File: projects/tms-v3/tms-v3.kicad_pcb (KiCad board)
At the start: 2 copper layers, 100 x 80 mm, 66 parts, among them J1 XT60-ELEC, J2 XT60-IGN, J3 LOAD-CELL, J4 PRESSURE, J5 ARM-SW, J6 E-MATCH, J7 TEENSY-L, J8 TEENSY-R, J9 XBEE3, K1 HF46F, Q1 MMBT3904, U2 ADS1256, U3 ADS1220, U4 LM7805, Y1 7.68MHz

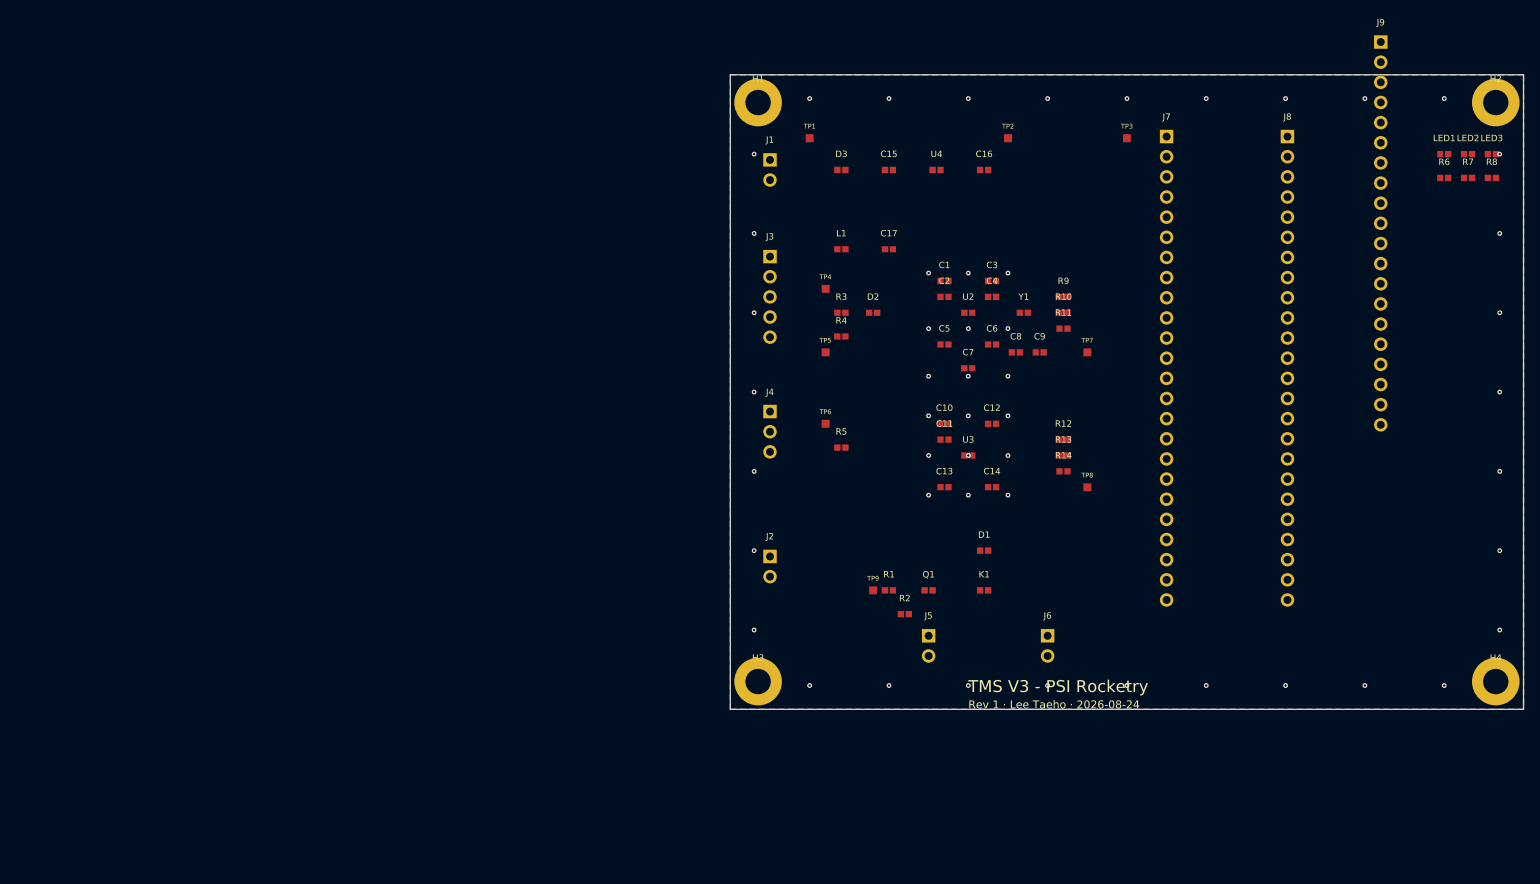
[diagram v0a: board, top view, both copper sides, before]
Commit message: PCB workspace: scoped escape hatch, hardened gates, repo cleanup
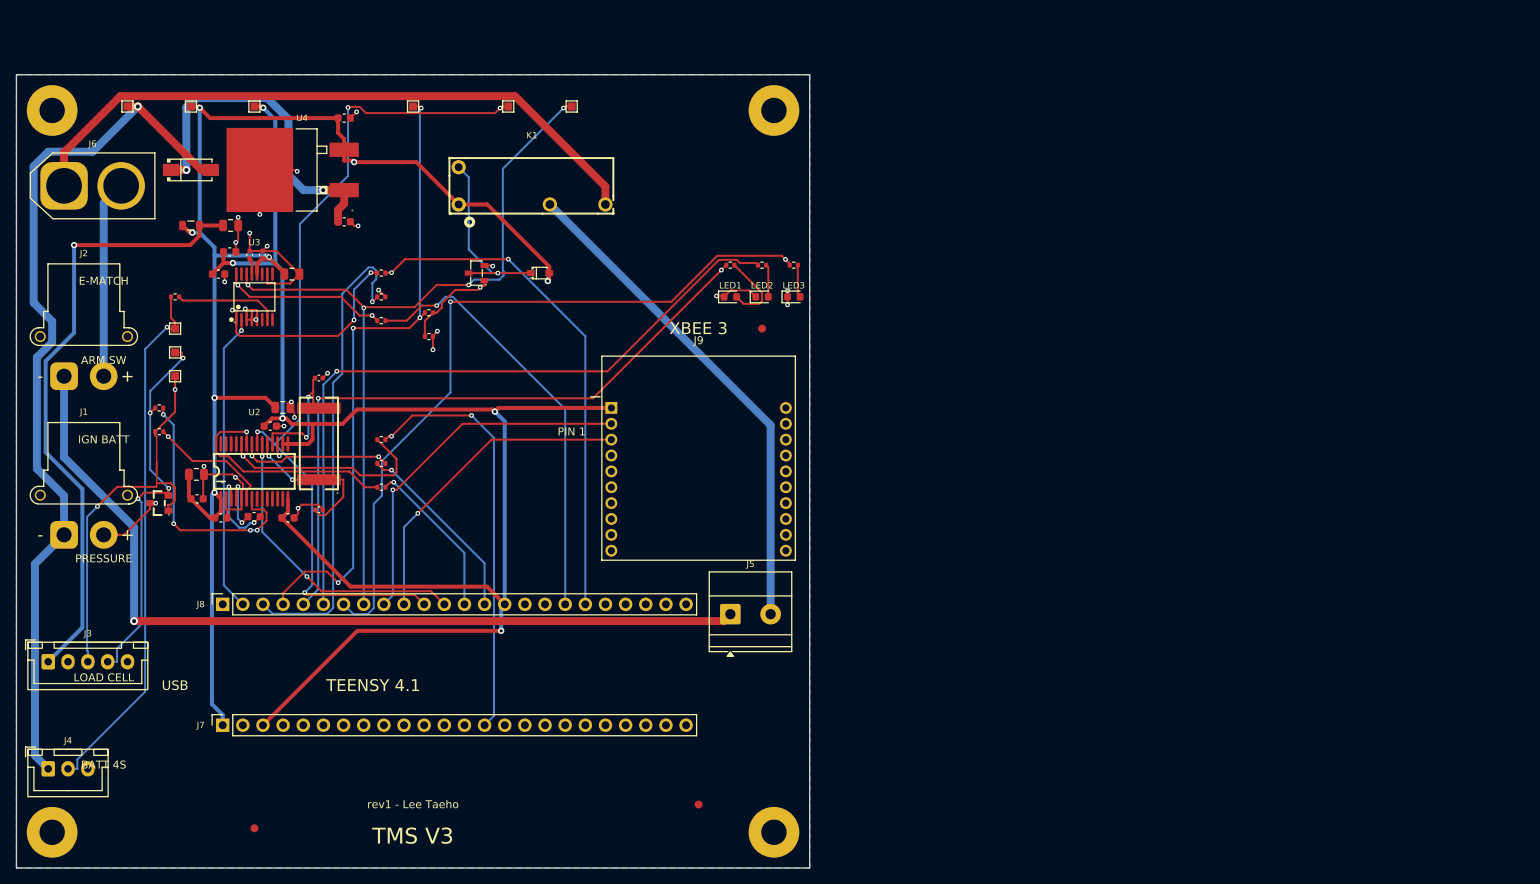
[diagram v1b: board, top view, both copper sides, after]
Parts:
- added FID1: FIDUCIAL, Fiducial:Fiducial_1mm_Mask3mm, F.Cu at (40.0, 195.0)
- added FID2: FIDUCIAL, Fiducial:Fiducial_1mm_Mask3mm, F.Cu at (96.0, 192.0)
- added FID3: FIDUCIAL, Fiducial:Fiducial_1mm_Mask3mm, F.Cu at (104.0, 132.0)
- C10, C11: footprint Capacitor_SMD:C_0603_1608Metric -> Capacitor_SMD:C_0402_1005Metric
- D1: footprint Diode_SMD:D_SOD-323 -> jlcpcb:SOD-323_L1.8-W1.3-LS2.5-RD-1
- D2: value TVS -> PESD5V0S2BT; footprint Package_TO_SOT_SMD:SOT-23 -> jlcpcb:SOT-23_L2.9-W1.3-P1.90-LS2.4-BR
- D3: footprint Diode_SMD:D_SMA -> jlcpcb:SMA_L4.4-W2.8-LS5.4-R-RD
- J1: value XT60-ELEC -> XT30PW-ELEC; footprint Connector_PinHeader_2.54mm:PinHeader_1x02_P2.54mm_Vertical -> Connector_AMASS:AMASS_XT30PW-F_1x02_P2.50mm_Horizontal
- J2: value XT60-IGN -> XT30PW-IGN; footprint Connector_PinHeader_2.54mm:PinHeader_1x02_P2.54mm_Vertical -> Connector_AMASS:AMASS_XT30PW-F_1x02_P2.50mm_Horizontal
- J3: footprint Connector_PinHeader_2.54mm:PinHeader_1x05_P2.54mm_Vertical -> Connector_JST:JST_XH_B5B-XH-A_1x05_P2.50mm_Vertical
- J4: footprint Connector_PinHeader_2.54mm:PinHeader_1x03_P2.54mm_Vertical -> Connector_JST:JST_XH_B3B-XH-A_1x03_P2.50mm_Vertical
- J5: footprint Connector_PinHeader_2.54mm:PinHeader_1x02_P2.54mm_Vertical -> TerminalBlock_Phoenix:TerminalBlock_Phoenix_MKDS-1,5-2-5.08_1x02_P5.08mm_Horizontal
- J6: value E-MATCH -> IGN-OUT; footprint Connector_PinHeader_2.54mm:PinHeader_1x02_P2.54mm_Vertical -> Connector_AMASS:AMASS_XT60-F_1x02_P7.20mm_Vertical
- J7, J8: footprint Connector_PinHeader_2.54mm:PinHeader_1x24_P2.54mm_Vertical -> Connector_PinSocket_2.54mm:PinSocket_1x24_P2.54mm_Vertical
- J9: value XBEE3 -> XBee_THT_20pin_P2.00mm; footprint Connector_PinHeader_2.54mm:PinHeader_2x10_P2.00mm_Vertical -> tms:XBee_THT_20pin_P2.00mm
- K1: value HF46F -> HF46F-G/5-HS1T; footprint Relay_THT:Relay_SPDT_HF46F -> jlcpcb:RELAYS-TH_HF46F-G-XX-HS1-XXX
- Q1: footprint Package_TO_SOT_SMD:SOT-23 -> jlcpcb:SOT-23-3_L2.9-W1.3-P1.90-LS2.4-BR
- U2: value ADS1256 -> ADS1256IDBR; footprint Package_SO:SSOP-28_5.3x10.2mm_P0.65mm -> jlcpcb:SSOP-28_L10.2-W5.3-P0.65-LS7.8-BL
- U3: value ADS1220 -> ADS1220IPWR; footprint Package_SO:TSSOP-16_4.4x5mm_P0.65mm -> jlcpcb:TSSOP-16_L5.0-W4.4-P0.65-LS6.4-BL
- U4: footprint Package_TO_SOT_SMD:TO-263-3_TabPin2 -> jlcpcb:TO-263-2_L10.1-W9.1-P5.08-LS15.2-BR-1
- Y1: footprint Crystal:Crystal_HC49-U_Vertical -> jlcpcb:CRYSTAL-SMD_L11.4-W4.7-LS12.4
- moved J8 137.5 mm to (36.0, 166.8), turned to 90 degrees
- moved J6 136.9 mm to (16.0, 114.0)
- moved J7 127.2 mm to (36.0, 182.0), turned to 90 degrees
- moved TP3 110.1 mm to (40.0, 104.0)
- moved C3 103.2 mm to (32.7, 150.4)
- moved TP2 103.1 mm to (32.0, 104.0)
- moved J3 102.0 mm to (14.0, 174.0)
- moved C14 101.2 mm to (35.5, 125.1)
- moved J4 100.4 mm to (14.0, 187.5)
- moved J1 100.2 mm to (16.0, 158.0)
- moved J9 99.5 mm to (85.0, 142.0)
- moved C2 97.6 mm to (32.8, 153.5)
- moved C1 96.0 mm to (35.8, 155.9)
- moved C13 94.9 mm to (36.9, 122.3)
- moved D2 93.1 mm to (28.0, 154.0)
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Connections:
- C11 pad 1: +5V -> +3V3
- C7 pad 1: (no net) -> VREF_P
- C7 pad 2: GND -> VREF_N
- C8 pad 1: GND -> XTAL1
- C9 pad 1: GND -> XTAL2
- D1 pad 1: (no net) -> RELAY_COIL_SW
- D1 pad 2: GND -> +5V
- D2 pad 1: (no net) -> LC_SIG_P
- D2 pad 2: GND -> LC_SIG_N
- D3 pad 1: VBAT_PROT -> VBAT
- D3 pad 2: GND -> VBAT_PROT
- H1 pad 1: GND -> (no net)
- H2 pad 1: GND -> (no net)
- H3 pad 1: GND -> (no net)
- H4 pad 1: GND -> (no net)
- J1 pad 1: (no net) -> VBAT
- J1 pad 2: (no net) -> GND
- J2 pad 1: (no net) -> IGN_BATT+
- J2 pad 2: (no net) -> IGN_GND
- J3 pad 1: (no net) -> +5V_FILT
- J3 pad 2: (no net) -> GND
- J3 pad 3: (no net) -> LC_SIG_P
- J3 pad 4: (no net) -> LC_SIG_N
- J3 pad 5: (no net) -> GND
- J4 pad 1: (no net) -> VBAT
- J4 pad 2: (no net) -> PRES_RAW
- J4 pad 3: (no net) -> GND
- J5 pad 1: (no net) -> IGN_BATT+
- J5 pad 2: (no net) -> IGN_ARM_RET
- J6 pad 1: (no net) -> IGN_OUT
- J6 pad 2: (no net) -> IGN_GND
- J7 pad 1: (no net) -> +5V
- J7 pad 14: (no net) -> SPI0_SCK
- J7 pad 15: (no net) -> GND
- J7 pad 2: (no net) -> GND
- J7 pad 3: (no net) -> +3V3
- J8 pad 1: (no net) -> GND
- J8 pad 10: (no net) -> UART2_TX
- J8 pad 11: (no net) -> ADS1256_DRDY
- J8 pad 12: (no net) -> ADS1256_CS
- J8 pad 13: (no net) -> SPI0_MOSI
- J8 pad 14: (no net) -> SPI0_MISO
- J8 pad 15: (no net) -> +3V3
- J8 pad 18: (no net) -> SPI1_MOSI
- J8 pad 19: (no net) -> SPI1_SCK
- J8 pad 2: (no net) -> ADS1220_CS
- J8 pad 3: (no net) -> SPI1_MISO
- J8 pad 4: (no net) -> RELAY_CTRL
- J8 pad 5: (no net) -> LED_PWR
- J8 pad 6: (no net) -> LED_ARM
- J8 pad 7: (no net) -> LED_TX
- J8 pad 8: (no net) -> ADS1220_DRDY
- J8 pad 9: (no net) -> UART2_RX
- J9 pad 1: (no net) -> +3V3
- J9 pad 10: (no net) -> GND
- J9 pad 2: (no net) -> UART2_RX
- J9 pad 3: (no net) -> UART2_TX
- K1 pad 1: (no net) -> +5V
- K1 pad 2: GND -> IGN_ARM_RET
- L1 pad 2: GND -> +5V_FILT
- LED1 pad 1: LED_PWR -> GND
- LED1 pad 2: GND -> LED_PWR_A
- LED2 pad 1: LED_ARM -> GND
- LED2 pad 2: GND -> LED_ARM_A
- LED3 pad 1: LED_TX -> GND
- LED3 pad 2: GND -> LED_TX_A
- Q1 pad 1: GND -> NPN_BASE
- R1 pad 2: GND -> NPN_BASE
- R10 pad 2: GND -> ADS1256_DOUT_ADC
- R11 pad 1: SPI0_SCK -> ADS1256_SCLK_ADC
- R11 pad 2: GND -> SPI0_SCK
- R12 pad 1: SPI1_MOSI -> ADS1220_DIN_ADC
- R12 pad 2: GND -> SPI1_MOSI
- R13 pad 2: GND -> ADS1220_DOUT_ADC
- R14 pad 1: SPI1_SCK -> ADS1220_SCLK_ADC
- R14 pad 2: GND -> SPI1_SCK
- R2 pad 1: GND -> NPN_BASE
- R3 pad 1: LC_AINP -> LC_SIG_P
- R3 pad 2: GND -> LC_AINP
- R4 pad 1: LC_AINN -> LC_SIG_N
- R4 pad 2: GND -> LC_AINN
- R5 pad 1: PRES_SIG -> PRES_RAW
- R5 pad 2: GND -> PRES_SIG
- R6 pad 2: GND -> LED_PWR_A
- R7 pad 2: GND -> LED_ARM_A
- R8 pad 2: GND -> LED_TX_A
- R9 pad 1: SPI0_MOSI -> ADS1256_DIN_ADC
- R9 pad 2: GND -> SPI0_MOSI
- TP4 pad 1: LC_AINP -> LC_SIG_P
- TP5 pad 1: LC_AINN -> LC_SIG_N
- TP6 pad 1: PRES_SIG -> PRES_RAW
- U2 pad 1: (no net) -> +5V
- U3 pad 1: (no net) -> ADS1220_SCLK_ADC
- U3 pad 2: GND -> ADS1220_CS
- U4 pad 1: +5V -> VBAT_PROT
- Y1 pad 1: (no net) -> XTAL1
- Y1 pad 2: GND -> XTAL2
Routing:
- net +3V3: track 0.00 -> 203.5 mm, vias 0 -> 5
- net +5V: track 0.00 -> 172.2 mm, vias 0 -> 7
- net VBAT: track 0.00 -> 111.4 mm, vias 0 -> 1
- net IGN_BATT+: track 0.00 -> 110.1 mm, vias 0 -> 1
- net ADS1256_DRDY: track 0.00 -> 108.3 mm, vias 0 -> 4
- net ADS1220_DRDY: track 0.00 -> 99.3 mm, vias 0 -> 4
- net LED_TX: track 0.00 -> 93.0 mm, vias 0 -> 2
- net LED_ARM: track 0.00 -> 89.3 mm, vias 0 -> 1
- net GND: track 0.00 -> 88.3 mm, vias 50 -> 26
- net LED_PWR: track 0.00 -> 85.2 mm, vias 0 -> 2
- net IGN_OUT: track 0.00 -> 82.4 mm
- net RELAY_CTRL: track 0.00 -> 80.4 mm, vias 0 -> 4
- net +5V_FILT: track 0.00 -> 78.3 mm, vias 0 -> 1
- net PRES_RAW: track 0.00 -> 66.8 mm, vias 0 -> 1
- net SPI1_SCK: track 0.00 -> 63.8 mm, vias 0 -> 2
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- removed copper zone on F.Cu, net GND
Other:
- board size 100 x 80 mm -> 100 x 100 mm
- rule pad_to_mask_clearance: 0.05 -> 0
- board text added: "ARM SW"
- board text added: "BATT 4S"
- board text added: "E-MATCH"
- board text added: "IGN BATT"
- board text added: "LOAD CELL"
- board text added: "PIN 1"
- board text added: "PRESSURE"
- board text added: "TEENSY 4.1"
- board text added: "TMS V3"
- board text added: "USB"
- board text added: "XBEE 3"
- board text added: "rev1 - Lee Taeho"
- board text removed: "ANALOG"
- board text removed: "DIGITAL"
- board text removed: "IGNITION"
- board text removed: "POWER"
- board text removed: "RF"
- board text removed: "Rev 1 · Lee Taeho · 2026-08-24"
- board text removed: "TMS V3 - PSI Rocketry"

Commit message: 9/6 update
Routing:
- net VBAT: track 111.4 -> 45.5 mm, vias 1 -> 0
- net PRES_RAW: track 66.8 -> 4.21 mm, vias 1 -> 0
- net ADS1220_DOUT_ADC: track 1.21 -> 20.1 mm, vias 1 -> 0
- net ADS1256_SCLK_ADC: track 27.2 -> 43.0 mm, vias 1 -> 2
- net LED_TX: track 93.0 -> 107.0 mm, vias 2 -> 3
- net ADS1256_DRDY: track 108.3 -> 98.4 mm
- net SPI0_SCK: track 52.8 -> 44.0 mm, vias 2 -> 1
- net LC_AINN: track 32.1 -> 25.8 mm, vias 4 -> 2
- net SPI1_SCK: track 63.8 -> 57.9 mm, vias 2 -> 1
- net SPI0_MISO: track 23.9 -> 28.8 mm
- net +3V3: track 203.5 -> 208.2 mm, vias 5 -> 6
- net ADS1256_CS: track 37.8 -> 42.5 mm
- net XTAL2: track 16.2 -> 12.7 mm, vias 2 -> 0
- net SPI1_MISO: track 60.5 -> 57.6 mm
- net UART2_TX: track 40.4 -> 43.1 mm
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
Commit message: feat: promote TMS hierarchy with safe board net reconciliation
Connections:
- net ADS1220_DIN_ADC renamed ADS1220 pressure/ADS1220_DIN_ADC
- net ADS1220_DOUT_ADC renamed ADS1220 pressure/ADS1220_DOUT_ADC
- net ADS1220_SCLK_ADC renamed ADS1220 pressure/ADS1220_SCLK_ADC
- net ADS1256_DIN_ADC renamed ADS1256 load cell/ADS1256_DIN_ADC
- net ADS1256_DOUT_ADC renamed ADS1256 load cell/ADS1256_DOUT_ADC
- net ADS1256_SCLK_ADC renamed ADS1256 load cell/ADS1256_SCLK_ADC
- net IGN_BATT+ renamed Connectors and test/IGN_BATT+
- net IGN_GND renamed Connectors and test/IGN_GND
- net LC_AINN renamed ADS1256 load cell/LC_AINN
- net LC_AINP renamed ADS1256 load cell/LC_AINP
- net LED_ARM renamed Controller and telemetry/LED_ARM
- net LED_ARM_A renamed Controller and telemetry/LED_ARM_A
- net LED_PWR renamed Controller and telemetry/LED_PWR
- net LED_PWR_A renamed Controller and telemetry/LED_PWR_A
- net LED_TX renamed Controller and telemetry/LED_TX
- net LED_TX_A renamed Controller and telemetry/LED_TX_A
- net NPN_BASE renamed Ignition/NPN_BASE
- net PRES_SIG renamed ADS1220 pressure/PRES_SIG
- net RELAY_COIL_SW renamed Ignition/RELAY_COIL_SW
- net UART2_RX renamed Controller and telemetry/UART2_RX
- net UART2_TX renamed Controller and telemetry/UART2_TX
- net VBAT_PROT renamed Power/VBAT_PROT
- net VREF_N renamed ADS1256 load cell/VREF_N
- net VREF_P renamed ADS1256 load cell/VREF_P
- net XTAL1 renamed ADS1256 load cell/XTAL1
- net XTAL2 renamed ADS1256 load cell/XTAL2

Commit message: batch
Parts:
- C8, C9: value 22pF -> 33pF
- J9: value XBee_THT_20pin_P2.00mm -> XBEE3
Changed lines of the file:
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@@
 			)
 		)
-		(property "Value" "22pF"
+		(property "Value" "33pF"
 			(at 0 1.16 0)
 			(layer "F.Fab")
@@
 			)
 		)
-		(property "LCSC Part" "C1663"
+		(property "LCSC Part" ""
 			(at 0 1.16 0)
 			(layer "F.Fab")
@@
 			)
 		)
-		(property "Value" "XBee_THT_20pin_P2.00mm"
+		(property "Value" "XBEE3"
 			(at 11 21 0)
 			(layer "F.Fab")
@@
 			)
 		)
-		(property "Value" "22pF"
+		(property "Value" "33pF"
 			(at 0 1.16 0)
 			(layer "F.Fab")
@@
 			)
 		)
-		(property "LCSC Part" "C1663"
+		(property "LCSC Part" ""
 			(at 0 1.16 0)
 			(layer "F.Fab")
